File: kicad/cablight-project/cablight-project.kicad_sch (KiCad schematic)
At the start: 14 parts, among them J3 Screw_Term_1x4_5mm, P1 Pololu D24V10F5, Q1 IRLB8721PBF, SW1 SW_DIP_x04, SW3 switch_SPDT_SLW_121586

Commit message: schematic USB-C, LDO, and MCU with rst + boot btns
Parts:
- added C1, C2: 22uF, cablight:_0805, symbol cablight-eagle-import:CAP_CERAMIC_0805
- added C3: 0u1F, cablight:_0805, symbol cablight-eagle-import:CAP_CERAMIC_0805
- added C4, C6, C7: 1uF, cablight:_0805, symbol cablight-eagle-import:CAP_CERAMIC_0805
- added C5: 10uF, cablight:_0805, symbol cablight-eagle-import:CAP_CERAMIC_0805
- added C8: 100nF, cablight:_0805, symbol cablight-eagle-import:CAP_CERAMIC_0805
- added D2: 1N5819, Diode_THT:D_DO-41_SOD81_P10.16mm_Horizontal, symbol Diode:1N5819
- added J1: USB_C_Receptacle_USB2.0_14P, symbol Connector:USB_C_Receptacle_USB2.0_14P
- added R2, R3: 10K, cablight:_0805, symbol cablight-eagle-import:RESISTOR_0805
- added R6, R7: 5K1, cablight:_0805, symbol cablight-eagle-import:RESISTOR_0805
- added SW2: BOOT, symbol Switch:SW_Push
- added SW4: RESET, symbol Switch:SW_Push
- added U2: AP2112K-3.3, Package_TO_SOT_SMD:SOT-23-5, symbol Regulator_Linear:AP2112K-3.3
- added U3: ESP32-S3-MINI-1U, RF_Module:ESP32-S2-MINI-1U, symbol RF_Module:ESP32-S3-MINI-1U
- added U4: USBLC6-2SC6, Package_TO_SOT_SMD:SOT-23-6, symbol Power_Protection:USBLC6-2SC6
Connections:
- net GND: now also BTN1.GND, C1.2, C2.2, C3.2, C4.2, C5.2, C6.2, C7.2, C8.2, J1.A1 (GND), J1.A12 (GND), J1.B1 (GND), J1.B12 (GND), J1.S1 (SHIELD), R6.2, R7.2, SW2.1, SW4.1, U2.2 (GND), U4.2 (GND)
- net SRO4 PWR: no longer R1.1
- new net: J1.A7 (D-), J1.B7 (D-), U4.1 (I/O1)
- new net: J1.A6 (D+), J1.B6 (D+), U4.3 (I/O2)
- new net: BTN1.1, R1.1
- new net: C7.1, R2.1, SW2.2, U3.4 (IO0)
- new net: C4.1, C6.1, R3.1, SW4.2, U3.45 (EN)
- new net: C8.1, D2.2 (A), J1.A4 (VBUS), J1.A9 (VBUS), J1.B4 (VBUS), J1.B9 (VBUS)
- new net: J1.A5 (CC1), R7.1
- new net: J1.B5 (CC2), R6.1
- new net: U3.1 (GND), U3.2 (GND), U3.42 (GND), U3.43 (GND), U3.46 (GND), U3.47 (GND), U3.48 (GND), U3.49 (GND), U3.50 (GND), U3.51 (GND), U3.52 (GND), U3.53 (GND), U3.54 (GND), U3.55 (GND), U3.56 (GND), U3.57 (GND), U3.58 (GND), U3.59 (GND), U3.60 (GND), U3.61 (GND), U3.62 (GND), U3.63 (GND), U3.64 (GND), U3.65 (GND)
- new net 3.3V: C1.1, C3.1, C5.1, R1.2, R2.2, R3.2, U2.5 (VOUT), U3.3 (3V3)
- new net 5V: C2.1, D2.1 (K), U2.1 (VIN), U2.3 (EN), U4.5 (VBUS)
- new net D+: U4.4 (I/O2)
- new net D-: U4.6 (I/O1)
- now unconnected: U1.11 (GPIO_35)
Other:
- note added: "3.3V LDO"
- note added: "MCU"
- note added: "This is for lower dropout voltage (0.2V) for usage with a battery. The AMS1117 chip is much cheaper, but with higher drop out voltage."
- note added: "USB-C"
- note added: "can also use SMD NSR0320"
- note added: "findo out what IO corresponts to what GPIO? I think I can pick which ones I want. Ties rest to GND."
- note added: "verify usb-c resistor requirements"
- moved on the sheet: BTN1, D1, J3, P1, Q1, R1, R4, R5, S1, SW1, SW3, TP1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

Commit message: select footprints. layout buck 5v converter
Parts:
- removed P1: Pololu D24V10F5, GRK_Lib:Pololu_5V_H, symbol user:Pololu_0J8557_24V
- removed S1: RCWL-1601, GRK_Lib:RCWL-1601, symbol user:RCWL-1601
- removed TP2: 5V, TestPoint:TestPoint_THTPad_D1.0mm_Drill0.5mm, symbol Connector:TestPoint
- removed U1: ~, GRK_Lib:AdafruitQTPyEsp32S3, symbol GRK_Global_Sym_Lib:Adafruit_QTPy_Esp32S3
- added C10: 100nF, Capacitor_SMD:C_0201_0603Metric, symbol cablight-eagle-import:CAP_CERAMIC_0805
- added C11, C13: 1uF, Capacitor_SMD:C_0201_0603Metric, symbol cablight-eagle-import:CAP_CERAMIC_0805
- added C11A1, C11B1, C11D1, C11E1, C11F1, C11G1: 10uF, Capacitor_SMD:C_0402_1005Metric, symbol cablight-eagle-import:CAP_CERAMIC_0805
- added C11C1: 10Uf, Capacitor_SMD:C_0402_1005Metric, symbol cablight-eagle-import:CAP_CERAMIC_0805
- added C12: 27pF, Capacitor_SMD:C_0201_0603Metric, symbol cablight-eagle-import:CAP_CERAMIC_0805
- added C9: 4.7uF, Capacitor_SMD:C_0402_1005Metric, symbol cablight-eagle-import:CAP_CERAMIC_0805
- added L1: 22uH, GRK_Lib:Wurth Inductor 22uH 1.15A 225mOhm, symbol Device:L
- added R10, R11: 100K, Resistor_SMD:R_0201_0603Metric, symbol cablight-eagle-import:RESISTOR_0805
- added R8: 91K, Resistor_SMD:R_0201_0603Metric, symbol cablight-eagle-import:RESISTOR_0805
- added R9: 12K4, Resistor_SMD:R_0201_0603Metric, symbol cablight-eagle-import:RESISTOR_0805
- added S2: RCWL-1601, GRK_Lib:Terminal Block 4-Pin 2mm Pitch, symbol user:RCWL-1601
- added T1: ISL85410, GRK_Lib:ISL85410, symbol GRK_Global_Sym_Lib:ISL85410
- C1, C2, C5: footprint cablight:_0805 -> Capacitor_SMD:C_0402_1005Metric
- C3, C4, C6, C7, C8: footprint cablight:_0805 -> Capacitor_SMD:C_0201_0603Metric
- J1: footprint (none) -> Connector_USB:USB_C_Receptacle_GCT_USB4105-xx-A_16P_TopMnt_Horizontal
- R1, R4, R5: footprint Resistor_SMD:R_0805_2012Metric_Pad1.20x1.40mm_HandSolder -> Resistor_SMD:R_0201_0603Metric
- R2, R3, R6, R7: footprint cablight:_0805 -> Resistor_SMD:R_0201_0603Metric
- SW2, SW4: footprint (none) -> GRK_Lib:Tactile Switch 6x6x7 SMD C69055
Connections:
- net 5V_MCU is gone; now on net 5V: D1.1 (K)
- net 3.3V: now also C13.1, S2.1 (Vin)
- net GND: now also Q1.3 (S), R4.2, SW1.1, SW1.2, SW1.3, C11.2, C11A1.2, C11B1.2, C11C1.2, C11D1.2, C11E1.2, C11F1.2, C11G1.2, C13.2, C9.2, R10.1, R9.1, S2.4 (GND), T1.13 (GND_PAD), T1.6 (PGND)
- net +5V: no longer names the net of SW3.1
- net +5V: now also C11A1.1, C11B1.1, C11C1.1, C11D1.1, C11E1.1, C11F1.1, C11G1.1, C12.1, L1.2, R8.2
- net 5V_sw: no longer names the net of D1.2 (A), SW3.2
- net SRO4 PWR: no longer names the net of SW1.5
- new net: C12.2, R8.1, R9.2, T1.10 (FB)
- new net: C11.1, T1.1 (SS), T1.11 (COMP), T1.12 (FS), T1.9 (VCC)
- new net: R10.2, T1.2 (SYNC)
- new net: C10.2, T1.3 (BOOT)
- new net: C10.1, L1.1, T1.5 (PHASE)
- new net: R11.1, T1.7 (EN)
- new net 24VDC: C9.1, R11.2, T1.4 (VIN)
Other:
- note added: "5V BUCK CONVERTER"
- note added: "Protection from USB 5V"
- note added: "i think I can make this 10K for cost"
- note removed: "ADAFRUIT QTPy ESP32-S3"
- note removed: "Pololu 5VDC Buck Converter"
- note removed: "verify usb-c resistor requirements"
- moved on the sheet: BTN1, C1, C2, C8, D1, D2, J1, J3, Q1, R1, R4, R5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

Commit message: bad schematic checkpoint
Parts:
- removed C1, C2: 22uF, Capacitor_SMD:C_0402_1005Metric, symbol cablight-eagle-import:CAP_CERAMIC_0805
- removed C10: 100nF, Capacitor_SMD:C_0201_0603Metric, symbol cablight-eagle-import:CAP_CERAMIC_0805
- removed C11: 1uF, Capacitor_SMD:C_0201_0603Metric, symbol cablight-eagle-import:CAP_CERAMIC_0805
- removed C11A1, C11B1, C11D1, C11E1, C11F1, C11G1: 10uF, Capacitor_SMD:C_0402_1005Metric, symbol cablight-eagle-import:CAP_CERAMIC_0805
- removed C11C1: 10Uf, Capacitor_SMD:C_0402_1005Metric, symbol cablight-eagle-import:CAP_CERAMIC_0805
- removed C12: 27pF, Capacitor_SMD:C_0201_0603Metric, symbol cablight-eagle-import:CAP_CERAMIC_0805
- removed C9: 4.7uF, Capacitor_SMD:C_0402_1005Metric, symbol cablight-eagle-import:CAP_CERAMIC_0805
- removed L1: 22uH, GRK_Lib:Wurth Inductor 22uH 1.15A 225mOhm, symbol Device:L
- removed R10, R11: 100K, Resistor_SMD:R_0201_0603Metric, symbol cablight-eagle-import:RESISTOR_0805
- removed R8: 91K, Resistor_SMD:R_0201_0603Metric, symbol cablight-eagle-import:RESISTOR_0805
- removed R9: 12K4, Resistor_SMD:R_0201_0603Metric, symbol cablight-eagle-import:RESISTOR_0805
- removed T1: ISL85410, GRK_Lib:ISL85410, symbol GRK_Global_Sym_Lib:ISL85410
- removed TP1: GND, TestPoint:TestPoint_THTPad_D1.0mm_Drill0.5mm, symbol Connector:TestPoint
- removed U2: AP2112K-3.3, Package_TO_SOT_SMD:SOT-23-5, symbol Regulator_Linear:AP2112K-3.3
- removed U3: ESP32-S3-MINI-1U, RF_Module:ESP32-S2-MINI-1U, symbol RF_Module:ESP32-S3-MINI-1U
- removed U4: USBLC6-2SC6, Package_TO_SOT_SMD:SOT-23-6, symbol Power_Protection:USBLC6-2SC6
- added D10: 1N5819, Diode_THT:D_DO-41_SOD81_P2.54mm_Vertical_KathodeUp, symbol Diode:1N5819
- added D3, D5: ESD321, GRK_Lib:ESD321_SOT5x3_DYA_TEX, symbol Diode:1N5819
- added D6, D7: LED, LED_SMD:LED_1206_3216Metric_Pad1.42x1.75mm_HandSolder, symbol Device:LED
- added F1: 8A, GRK_Lib:Fuse SMD pkg 0679L, symbol Device:Fuse_Small
- added R14: 470, Resistor_SMD:R_0402_1005Metric, symbol Device:R
- added R16: 470, Resistor_SMD:R_0402_1005Metric, symbol cablight-eagle-import:RESISTOR_0805
- added TP2: 3V3, TestPoint:TestPoint_THTPad_D1.0mm_Drill0.5mm, symbol Connector:TestPoint
- added U3: ESP32-C6, GRK_Lib:ESP32-S3-WROOM-1U, symbol Espressif:ESP32-S3-WROOM-1
- BTN_BOOT1: renamed from SW2; value BOOT -> tactile; footprint GRK_Lib:Tactile Switch 6x6x7 SMD C69055 -> GRK_Lib:tactile Eswitch TL3365
- BTN_RESET1: renamed from SW4; value RESET -> Tactile; footprint GRK_Lib:Tactile Switch 6x6x7 SMD C69055 -> GRK_Lib:tactile Eswitch TL3365
- C13, C3, C4, C6, C7, C8: footprint Capacitor_SMD:C_0201_0603Metric -> Capacitor_SMD:C_0402_1005Metric_Pad0.74x0.62mm_HandSolder
- C5: footprint Capacitor_SMD:C_0402_1005Metric -> Capacitor_SMD:C_0402_1005Metric_Pad0.74x0.62mm_HandSolder
- D1: value 1N5817 -> 1N5819
- D2: footprint Diode_THT:D_DO-41_SOD81_P10.16mm_Horizontal -> Diode_THT:D_DO-41_SOD81_P2.54mm_Vertical_KathodeUp
- J1: footprint Connector_USB:USB_C_Receptacle_GCT_USB4105-xx-A_16P_TopMnt_Horizontal -> GRK_Lib:usbc-GCT_USB4160-03-0170-C_REVA2; symbol Connector:USB_C_Receptacle_USB2.0_14P -> GRK_Global_Sym_Lib:USB_C_Receptacle_USB2.0_14P
- Q1: footprint GRK_Lib:TO-220F-3_H_Heatsink -> Package_TO_SOT_SMD:TO-252-2
- R1, R2, R3, R4, R5: footprint Resistor_SMD:R_0201_0603Metric -> Resistor_SMD:R_0402_1005Metric
- R6, R7: footprint Resistor_SMD:R_0201_0603Metric -> Resistor_SMD:R_0805_2012Metric_Pad1.20x1.40mm_HandSolder
- renumbered BTN1 to BTN4
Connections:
- net 24VDC: now also D1.2 (A), J3.2 (Pin_2), D10.1 (K), F1.1
- net 3.3V: now also D6.2 (A), TP2.1, U3.2 (3V3)
- net 5V: now also SW3.2; no longer D1.1 (K)
- net D+: now also J1.A6 (D+), J1.B6 (D+), D3.2 (A), U3.14 (GPIO20/U1CTS/ADC2_CH9/CLK_OUT1/USB_D+)
- net D-: now also J1.A7 (D-), J1.B7 (D-), D5.2 (A), U3.13 (GPIO19/U1RTS/ADC2_CH8/CLK_OUT2/USB_D-)
- net GND: now also D3.1 (K), D5.1 (K), R14.2, R16.2, U3.1 (GND), U3.40 (GND), U3.41 (GND)
- net at SW3.1: now also D1.1 (K)
- net TRIG: now reaches S2.2 (Trig)
- net ECHO: now reaches S2.3 (Echo)
- net BTN: now reaches BTN4.1, R1.1
- net at BTN_BOOT1.2, C7.1, R2.1: now also U3.27 (GPIO0/BOOT)
- net PG: now reaches BTN_RESET1.2, C4.1, C6.1, R3.1
- net PG: now also U3.3 (EN)
- net LEDSIG: now reaches R4.1, R5.1, SW1.4
- net DIP4: now reaches SW1.5
- net DIP3: now reaches SW1.6
- net DIP2: now reaches SW1.7
- net DIP1: now reaches SW1.8
- net +24V: no longer names the net of J3.3 (Pin_3)
- net +24V: now also F1.2; no longer J3.2 (Pin_2)
- new net: D7.2 (A), R16.1
- new net: D10.2 (A), D7.1 (K)
- new net: D6.1 (K), R14.1
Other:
- note added: "PG is pulled low when power supply is out of spec."
- note added: "PWR SUPPLY ON INDICATOR (GREEN)"
- note added: "REVERSE POLARITY PWER CONNECTION WILL DESTROY USB HOST"
- note added: "Reverse Polarity Indicator"
- note added: "SENSORS & BUTTONS"
- note added: "ULTRASONIC DISTANCE SENSOR RCWL-1601 (HC-SR04 Compatible)"
- note added: "i may forgo esd protection as usb plugging duty cycle isn't high enough for likely wrongful insertions. USB is only for flashing & debugging."
- note added: "todo: do calculation of debounce time with cap val"
- note removed: "3.3V LDO"
- note removed: "Protection from USB 5V"
- note removed: "This is for lower dropout voltage (0.2V) for usage with a battery. The AMS1117 chip is much cheaper, but with higher drop out voltage."
- note removed: "ULTRASONIC DISTANCE SENSOR RCWL-1601 (HC-SR04)"
- note removed: "i think I can make this 10K for cost"
- moved on the sheet: BTN4, BTN_BOOT1, BTN_RESET1, C13, C3, C4, C5, C6, C7, C8, D1, D2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

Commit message: fixed missing symbols
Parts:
- added C10: 100nF, Capacitor_SMD:C_0402_1005Metric, symbol cablight-eagle-import:CAP_CERAMIC_0805
- added C11: 1uF, Capacitor_SMD:C_0402_1005Metric, symbol cablight-eagle-import:CAP_CERAMIC_0805
- added C11A1, C11B1, C11D1, C11E1, C11F1, C11G1: 10uF, Capacitor_SMD:C_0402_1005Metric, symbol cablight-eagle-import:CAP_CERAMIC_0805
- added C11C1: 10Uf, Capacitor_SMD:C_0402_1005Metric, symbol cablight-eagle-import:CAP_CERAMIC_0805
- added C12: 27pF, Capacitor_SMD:C_0402_1005Metric, symbol cablight-eagle-import:CAP_CERAMIC_0805
- added C9: 4.7uF, Capacitor_SMD:C_0402_1005Metric, symbol cablight-eagle-import:CAP_CERAMIC_0805
- added L1: 22uH, GRK_Lib:Wurth Inductor 22uH 1.15A 225mOhm, symbol Device:L
- added R10, R11, R8: 100K, Resistor_SMD:R_0402_1005Metric, symbol cablight-eagle-import:RESISTOR_0805
- added R9: 22K1, Resistor_SMD:R_0402_1005Metric, symbol cablight-eagle-import:RESISTOR_0805
- added T1: ISL85410, GRK_Lib:ISL85410, symbol GRK_Global_Sym_Lib:ISL85410
- C13, C5, C6, C7, C8: footprint Capacitor_SMD:C_0402_1005Metric_Pad0.74x0.62mm_HandSolder -> Capacitor_SMD:C_0402_1005Metric
- C3, C4: footprint Capacitor_SMD:C_0402_1005Metric_Pad0.74x0.62mm_HandSolder -> Capacitor_SMD:C_0201_0603Metric
- Q1: footprint Package_TO_SOT_SMD:TO-252-2 -> GRK_Lib:TO-220F-3_H_Heatsink
- SW3: footprint GRK_Lib:Switch_SPDT_CUI_500mA_3mm -> Connector_PinHeader_2.54mm:PinHeader_1x02_P2.54mm_Vertical; symbol user:switch_SPDT_SLW_121586 -> Jumper:Jumper_2_Bridged
- U3: value ESP32-C6 -> ESP32-S3-WROOM-1U
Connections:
- net 3.3V: now also C11A1.1, C11B1.1, C11C1.1, C11D1.1, C11E1.1, C11F1.1, C11G1.1, C12.1, L1.2, R8.2
- net 5V: now also C9.1, R11.2, T1.4 (VIN)
- net GND: now also C11.2, C11A1.2, C11B1.2, C11C1.2, C11D1.2, C11E1.2, C11F1.2, C11G1.2, C9.2, R10.1, R9.1, T1.13 (GND_PAD), T1.6 (PGND)
- net PG: now also T1.8 (PG)
- new net: C12.2, R8.1, R9.2, T1.10 (FB)
- new net: C11.1, T1.1 (SS), T1.11 (COMP), T1.12 (FS), T1.9 (VCC)
- new net: R10.2, T1.2 (SYNC)
- new net: C10.2, T1.3 (BOOT)
- new net: C10.1, L1.1, T1.5 (PHASE)
- new net: R11.1, T1.7 (EN)
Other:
- note removed: "REVERSE POLARITY PWER CONNECTION WILL DESTROY USB HOST"
- moved on the sheet: D1, D2

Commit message: progress
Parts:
- renumbered BTN_BOOT1 to BOOT1, BTN4 to BTN1, SW1 to DIP1, D6 to LED-OK1, D7 to LED-W1, S2 to RCWL-1601, BTN_RESET1 to RESET1, J1 to USBC-V1
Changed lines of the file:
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@@
 		(on_board yes)
 		(dnp no)
-		(property "Reference" "S2"
+		(property "Reference" "RCWL-1601"
 			(at 160.782 36.322 0)
 			(effects
@@
 			(project "cablight-project"
 				(path "/2aa36568-293b-470b-bbef-a9ff44d0879c"
-					(reference "S2")
+					(reference "RCWL-1601")
 					(unit 1)
 				)
@@
 		(dnp no)
 		(fields_autoplaced yes)
-		(property "Reference" "BTN4"
+		(property "Reference" "BTN1"
 			(at 43.18 35.56 0)
 			(effects
@@
 			(project "cablight-project"
 				(path "/2aa36568-293b-470b-bbef-a9ff44d0879c"
-					(reference "BTN4")
+					(reference "BTN1")
 					(unit 1)
 				)
@@
 		(dnp no)
 		(fields_autoplaced yes)
-		(property "Reference" "BTN_BOOT1"
+		(property "Reference" "BOOT1"
 			(at 407.67 87.63 0)
 			(effects
@@
 			(project ""
 				(path "/2aa36568-293b-470b-bbef-a9ff44d0879c"
-					(reference "BTN_BOOT1")
+					(reference "BOOT1")
 					(unit 1)
 				)
@@
 		(dnp no)
 		(fields_autoplaced yes)
-		(property "Reference" "BTN_RESET1"
+		(property "Reference" "RESET1"
 			(at 229.87 50.8 0)
 			(effects
@@
 			(project "cablight-project"
 				(path "/2aa36568-293b-470b-bbef-a9ff44d0879c"
-					(reference "BTN_RESET1")
+					(reference "RESET1")
 					(unit 1)
 				)
@@
 		(dnp no)
 		(fields_autoplaced yes)
-		(property "Reference" "SW1"
+		(property "Reference" "DIP1"
 			(at 82.55 29.21 0)
 			(effects
@@
 			(project ""
 				(path "/2aa36568-293b-470b-bbef-a9ff44d0879c"
-					(reference "SW1")
+					(reference "DIP1")
 					(unit 1)
 				)
@@
 		(on_board yes)
 		(dnp no)
-		(property "Reference" "D7"
+		(property "Reference" "LED-W1"
 			(at 74.93 228.2825 0)
 			(effects
@@
 			(project "cablight-project"
 				(path "/2aa36568-293b-470b-bbef-a9ff44d0879c"
-					(reference "D7")
+					(reference "LED-W1")
 					(unit 1)
 				)
@@
 		(on_board yes)
 		(dnp no)
-		(property "Reference" "J1"
-			(at 31.75 127 0)
+		(property "Reference" "USBC-V1"
+			(at 27.178 124.968 0)
 			(effects
 				(font
@@
 			(project ""
 				(path "/2aa36568-293b-470b-bbef-a9ff44d0879c"
-					(reference "J1")
+					(reference "USBC-V1")
 					(unit 1)
 				)
@@
 		(on_board yes)
 		(dnp no)
-		(property "Reference" "D6"
+		(property "Reference" "LED-OK1"
 			(at 249.682 223.52 90)
 			(effects
@@
 			(project ""
 				(path "/2aa36568-293b-470b-bbef-a9ff44d0879c"
-					(reference "D6")
+					(reference "LED-OK1")
 					(unit 1)
 				)

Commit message: 80 percent layout v1
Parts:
- added R12, R13: 2M, Resistor_SMD:R_0805_2012Metric_Pad1.20x1.40mm_HandSolder, symbol cablight-eagle-import:RESISTOR_0805
- C10, C11, C11A1, C11B1, C11C1, C11D1, C11E1, C11F1, C11G1, C12, C13, C5, C6, C7, C8, C9: footprint Capacitor_SMD:C_0402_1005Metric -> Capacitor_SMD:C_0805_2012Metric_Pad1.18x1.45mm_HandSolder
- C3, C4: footprint Capacitor_SMD:C_0201_0603Metric -> Capacitor_SMD:C_0805_2012Metric_Pad1.18x1.45mm_HandSolder
- R1, R10, R11, R14, R16, R2, R3, R4, R5, R8, R9: footprint Resistor_SMD:R_0402_1005Metric -> Resistor_SMD:R_0805_2012Metric_Pad1.20x1.40mm_HandSolder
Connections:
- net BTN: now also U3.38 (GPIO2/TOUCH2/ADC1_CH1)
- net DIP1: now also U3.10 (GPIO17/U1TXD/ADC2_CH6)
- net DIP2: now also U3.11 (GPIO18/U1RXD/ADC2_CH7/CLK_OUT3)
- net DIP3: now also U3.18 (GPIO10/TOUCH10/ADC1_CH9/FSPICS0/FSPIIO4/SUBSPICS0)
- net DIP4: now also U3.17 (GPIO9/TOUCH9/ADC1_CH8/FSPIHD/SUBSPIHD)
- net ECHO: now also U3.21 (GPIO13/TOUCH13/ADC2_CH2/FSPIQ/FSPIIO7/SUBSPIQ)
- net GND: now also R12.2, R13.2
- net LEDSIG: now also U3.5 (GPIO5/TOUCH5/ADC1_CH4)
- net TRIG: now also U3.22 (GPIO14/TOUCH14/ADC2_CH3/FSPIWP/FSPIDQS/SUBSPIWP)
- net VBUS: now reaches C8.1, D2.2 (A), USBC-V1.A4 (VBUS), USBC-V1.A9 (VBUS), USBC-V1.B4 (VBUS), USBC-V1.B9 (VBUS)
- net LED+: now reaches F1.2, J3.3 (Pin_3)
- net at USBC-V1.A8 (SBU1): now also R13.1
- net at USBC-V1.B8 (SBU2): now also R12.1
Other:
- note added: "CONSULT DATASHEET FOR IMPORTANT UART PINS ETC"
- note added: "TODO: weak pulldown to gnd? for sbu pins?"
- moved on the sheet: C8, D2, D3, D5, R6, R7

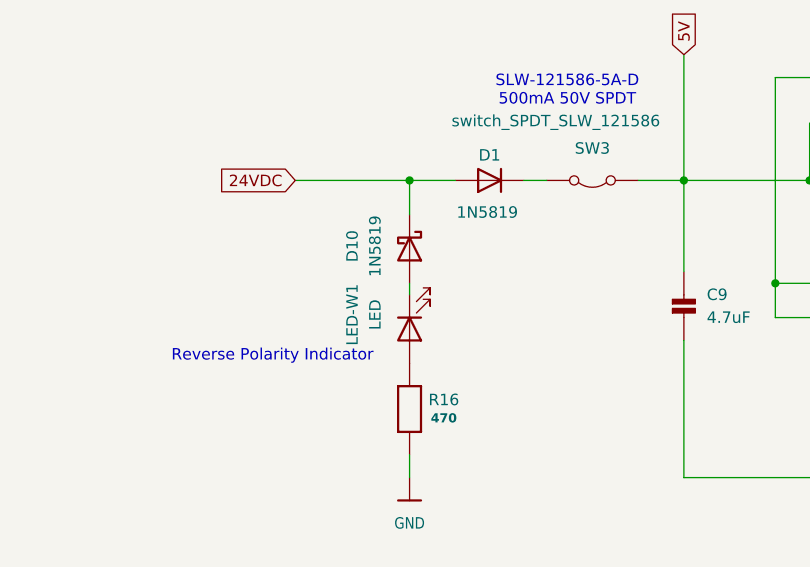
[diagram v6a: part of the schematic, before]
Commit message: change fuse pkg & add datasheets
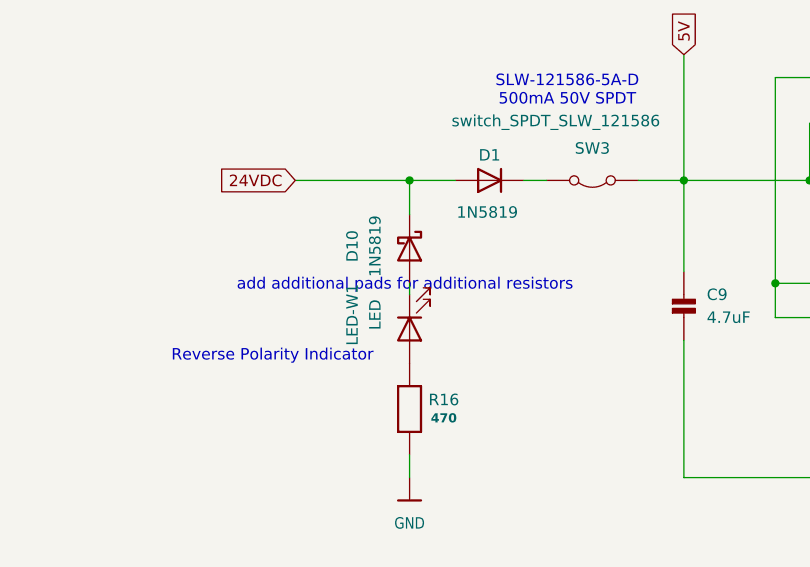
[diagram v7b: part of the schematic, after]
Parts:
- F1: footprint GRK_Lib:Fuse SMD pkg 0679L -> Fuse:Fuse_1206_3216Metric_Pad1.42x1.75mm_HandSolder
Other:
- note added: "add additional pads for additional resistors"

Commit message: progress
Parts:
- added R15, R17: 0, Resistor_SMD:R_0805_2012Metric_Pad1.20x1.40mm_HandSolder, symbol cablight-eagle-import:RESISTOR_0805
- C6, C7: value 1uF -> 0u1F
- renumbered C13 to C14, C11A1 to CP1, C11B1 to CP2, C11C1 to CP3, C11D1 to CP4, C11E1 to CP5, C11F1 to CP6, C11G1 to CP7
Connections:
- net GND: now also R15.2, R17.2; no longer R14.2, R16.2
- new net: R15.1, R16.2
- new net: R14.2, R17.1
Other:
- note added: "findo out what IO corresponts to what GPIO? I think I can pick which ones I want."
- note removed: "findo out what IO corresponts to what GPIO? I think I can pick which ones I want. Ties rest to GND."
- note removed: "todo: do calculation of debounce time with cap val"
- moved on the sheet: C4, LED-OK1, R14
